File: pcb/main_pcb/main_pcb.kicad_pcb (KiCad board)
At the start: 2 copper layers, 80 x 100 mm, 72 parts, among them J1 Conn_01x05, J10 Conn_01x06_Male, J11 Conn_01x04, J12 Screw_Terminal_01x02, J13 Conn_01x02_Male, J2 Conn_01x05, J3 Conn_01x05, J4 Conn_01x05, J5 Conn_01x05, J6 Conn_01x05, J7 Conn_01x04, J8 Conn_01x06_Male, J9 Conn_01x04, Q1 Q_PMOS_GDS, SW1 SW_SPDT, U1 LSM6DSO, U2 Teensy_4.1, U3 DRV8833, U4 LM1117-3.3, U5 TPIC74101

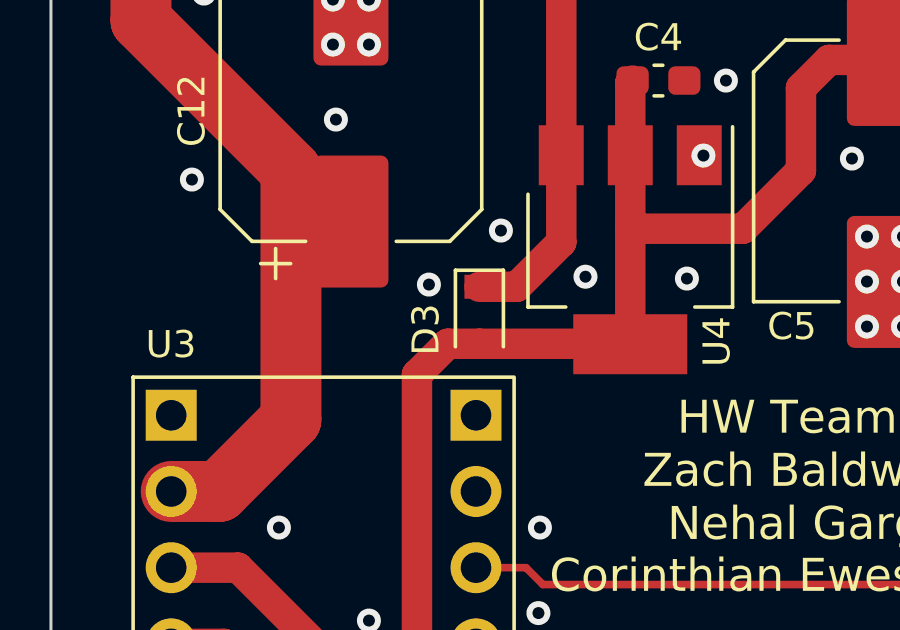
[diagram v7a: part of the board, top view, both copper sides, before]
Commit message: Change 3V3 reg reverse diode footprint
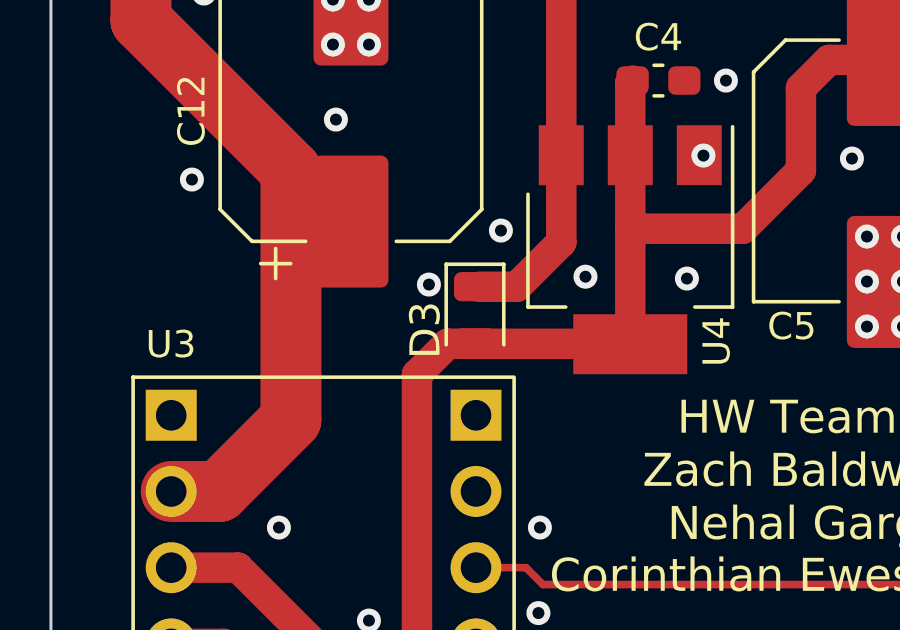
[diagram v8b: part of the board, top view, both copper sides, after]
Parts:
- D3: footprint Diode_SMD:D_SOD-110 -> Diode_SMD:D_0805_2012Metric
- moved D3 0.15 mm to (64.1, 114.8)
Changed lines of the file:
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@@
     )
   )
-  (footprint "Diode_SMD:D_SOD-110" (layer "F.Cu")
-    (at 64.2825 114.8232 -90)
-    (descr "SOD-110")
-    (tags "SOD-110")
+  (footprint "Diode_SMD:D_0805_2012Metric" (layer "F.Cu")
+    (at 64.135 114.808 -90)
+    (descr "Diode SMD 0805 (2012 Metric), square (rectangular) end terminal, IPC_7351 nominal, (Body size source: https://docs.google.com/spreadsheets/d/1BsfQQcO9C6DZCsRaXUlFlo91Tg2WpOkGARC1WS5S8t0/edit?usp=sharing), generated with kicad-footprint-generator")
+    (tags "diode")
     (property "Sheetfile" "power_supply.kicad_sch")
     (property "Sheetname" "Power Supply")
     (attr smd)
-    (fp_text reference "D3" (at 0.4768 1.7825 90) (layer "F.SilkS")
-      (effects (font (size 0.9 0.9) (thickness 0.14)))
-    )
-    (fp_text value "D" (at 0 1.8 90) (layer "F.Fab")
+    (fp_text reference "D3" (at 0.508 1.651 -90) (layer "F.SilkS")
       (effects (font (size 1 1) (thickness 0.15)))
     )
-    (fp_text user "${REFERENCE}" (at 0 -1.7 90) (layer "F.Fab")
+    (fp_text value "D" (at 0 1.65 -90) (layer "F.Fab")
       (effects (font (size 1 1) (thickness 0.15)))
     )
-    (fp_line (start -1.5 -0.8) (end 1.05 -0.8) (layer "F.SilkS") (width 0.12))
-    (fp_line (start -1.5 -0.8) (end -1.5 0.8) (layer "F.SilkS") (width 0.12))
-    (fp_line (start -1.5 0.8) (end 1.05 0.8) (layer "F.SilkS") (width 0.12))
-    (fp_line (start 1.6 1) (end -1.6 1) (layer "F.CrtYd") (width 0.05))
-    (fp_line (start -1.6 -1) (end 1.6 -1) (layer "F.CrtYd") (width 0.05))
-    (fp_line (start -1.6 -1) (end -1.6 1) (layer "F.CrtYd") (width 0.05))
-    (fp_line (start 1.6 -1) (end 1.6 1) (layer "F.CrtYd") (width 0.05))
-    (fp_line (start 0.1 -0.2) (end -0.2 0) (layer "F.Fab") (width 0.1))
-    (fp_line (start -0.2 0.2) (end -0.2 -0.2) (layer "F.Fab") (width 0.1))
-    (fp_line (start 0.1 0.2) (end 0.1 -0.2) (layer "F.Fab") (width 0.1))
-    (fp_line (start 1.05 -0.7) (end -1.05 -0.7) (layer "F.Fab") (width 0.1))
-    (fp_line (start 0.1 0) (end 0.25 0) (layer "F.Fab") (width 0.1))
-    (fp_line (start -1.05 -0.7) (end -1.05 0.7) (layer "F.Fab") (width 0.1))
-    (fp_line (start -1.05 0.7) (end 1.05 0.7) (layer "F.Fab") (width 0.1))
-    (fp_line (start -0.2 0) (end -0.35 0) (layer "F.Fab") (width 0.1))
-    (fp_line (start -0.2 0) (end 0.1 0.2) (layer "F.Fab") (width 0.1))
-    (fp_line (start 1.05 0.7) (end 1.05 -0.7) (layer "F.Fab") (width 0.1))
-    (pad "1" smd rect (at -0.95 0 270) (size 0.8 1) (layers "F.Cu" "F.Paste" "F.Mask")
+    (fp_text user "${REFERENCE}" (at 0 0 -90) (layer "F.Fab")
+      (effects (font (size 0.5 0.5) (thickness 0.08)))
+    )
+    (fp_line (start -1.685 0.96) (end 1 0.96) (layer "F.SilkS") (width 0.12))
+    (fp_line (start 1 -0.96) (end -1.685 -0.96) (layer "F.SilkS") (width 0.12))
+    (fp_line (start -1.685 -0.96) (end -1.685 0.96) (layer "F.SilkS") (width 0.12))
+    (fp_line (start 1.68 -0.95) (end 1.68 0.95) (layer "F.CrtYd") (width 0.05))
+    (fp_line (start -1.68 0.95) (end -1.68 -0.95) (layer "F.CrtYd") (width 0.05))
+    (fp_line (start 1.68 0.95) (end -1.68 0.95) (layer "F.CrtYd") (width 0.05))
+    (fp_line (start -1.68 -0.95) (end 1.68 -0.95) (layer "F.CrtYd") (width 0.05))
+    (fp_line (start 1 0.6) (end 1 -0.6) (layer "F.Fab") (width 0.1))
+    (fp_line (start -1 0.6) (end 1 0.6) (layer "F.Fab") (width 0.1))
+    (fp_line (start -1 -0.3) (end -1 0.6) (layer "F.Fab") (width 0.1))
+    (fp_line (start -0.7 -0.6) (end -1 -0.3) (layer "F.Fab") (width 0.1))
+    (fp_line (start 1 -0.6) (end -0.7 -0.6) (layer "F.Fab") (width 0.1))
+    (pad "1" smd roundrect (at -0.9375 0 270) (size 0.975 1.4) (layers "F.Cu" "F.Paste" "F.Mask") (roundrect_rratio 0.25)
       (net 11 "+5V") (pinfunction "K") (pintype "passive"))
-    (pad "2" smd rect (at 0.95 0 270) (size 0.8 1) (layers "F.Cu" "F.Paste" "F.Mask")
+    (pad "2" smd roundrect (at 0.9375 0 270) (size 0.975 1.4) (layers "F.Cu" "F.Paste" "F.Mask") (roundrect_rratio 0.25)
       (net 4 "+3V3") (pinfunction "A") (pintype "passive"))
-    (model "${KICAD6_3DMODEL_DIR}/Diode_SMD.3dshapes/D_SOD-110.wrl"
+    (model "${KICAD6_3DMODEL_DIR}/Diode_SMD.3dshapes/D_0805_2012Metric.wrl"
       (offset (xyz 0 0 0))
       (scale (xyz 1 1 1))
